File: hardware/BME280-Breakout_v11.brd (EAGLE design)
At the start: 20 x 20 mm, 23 parts, among them IC1 BME280, IC2 LDO-TS9011-3V3, J1 JUMPER2-0603, T1 BSS138PS, T2 BSS138PS, X1 PASSER-07, X2 PASSER-07

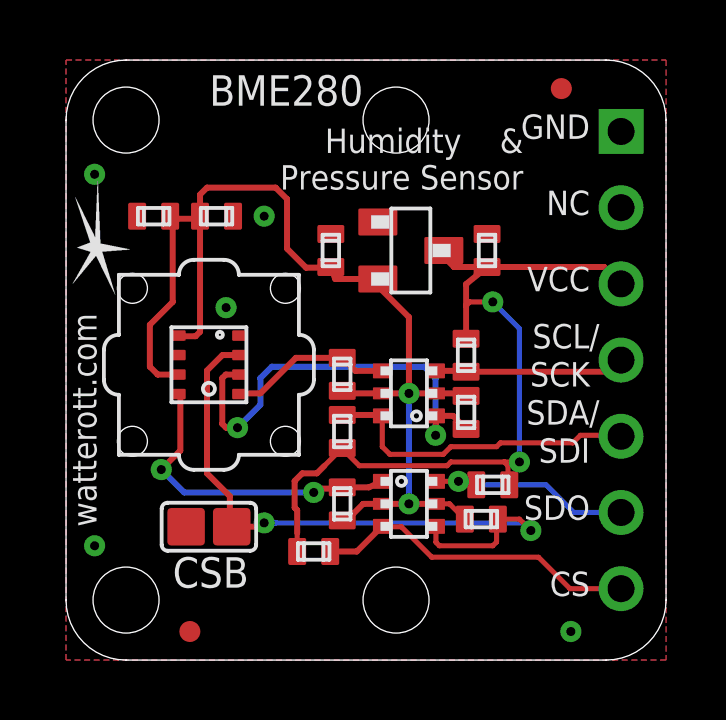
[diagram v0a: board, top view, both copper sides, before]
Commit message: updated schematics
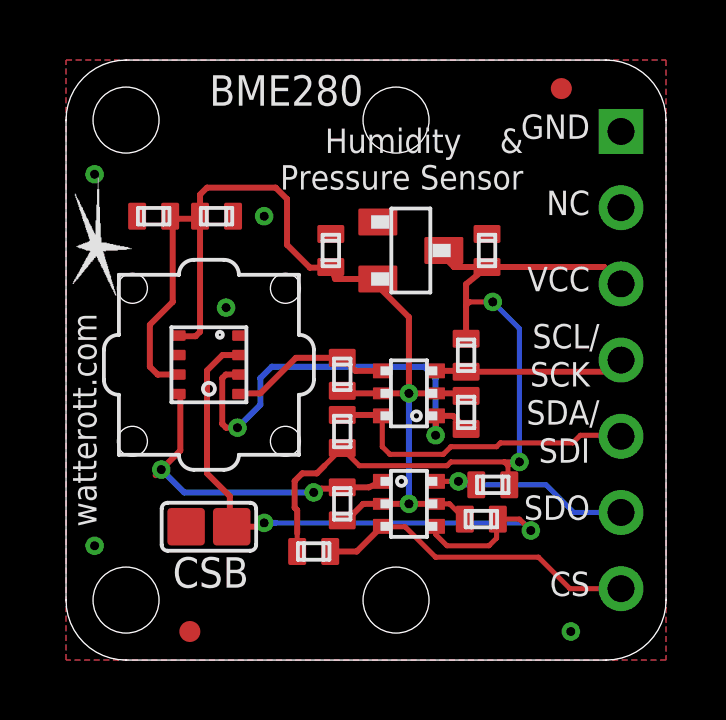
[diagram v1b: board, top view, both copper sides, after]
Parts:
- removed LOGO1: LOGO-S_PLACE_S, we-symbol:SPARK_TPLACE_S
- added LOGO3: LOGO_SPARK-2, we-symbol:SPARK_2MM
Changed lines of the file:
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@@
 <setting verticaltext="up"/>
 </settings>
-<grid distance="0.127" unitdist="mm" unit="mm" style="lines" multiple="1" display="yes" altdistance="0.0125" altunitdist="inch" altunit="inch"/>
+<grid distance="1.27" unitdist="mm" unit="inch" style="lines" multiple="1" display="yes" altdistance="0.0125" altunitdist="inch" altunit="inch"/>
 <layers>
 <layer number="1" name="Top" color="4" fill="1" visible="yes" active="yes"/>
@@
 </class>
 </classes>
-<designrules name="default *">
-<description language="de">&lt;b&gt;EAGLE Design Rules&lt;/b&gt;
-&lt;p&gt;
-Die Standard-Design-Rules sind so gewählt, dass sie für
-die meisten Anwendungen passen. Sollte ihre Platine
-besondere Anforderungen haben, treffen Sie die erforderlichen
-Einstellungen hier und speichern die Design Rules unter
-einem neuen Namen ab.</description>
-<description language="en">&lt;b&gt;EAGLE Design Rules&lt;/b&gt;
-&lt;p&gt;
-The default Design Rules have been set to cover
-a wide range of applications. Your particular design
-may have different requirements, so please make the
-necessary adjustments and save your customized
-design rules under a new name.</description>
+<designrules name="we-dru-2-layer *">
+<description language="de">&lt;b&gt;2 Layer PCB Design Rules&lt;/b&gt;</description>
+<description language="en">&lt;b&gt;2 Layer PCB Design Rules&lt;/b&gt;</description>
 <param name="layerSetup" value="(1*16)"/>
 <param name="mtCopper" value="0.035mm 0.035mm 0.035mm 0.035mm 0.035mm 0.035mm 0.035mm 0.035mm 0.035mm 0.035mm 0.035mm 0.035mm 0.035mm 0.035mm 0.035mm 0.035mm"/>
 <param name="mtIsolate" value="1.5mm 0.15mm 0.2mm 0.15mm 0.2mm 0.15mm 0.2mm 0.15mm 0.2mm 0.15mm 0.2mm 0.15mm 0.2mm 0.15mm 0.2mm"/>
-<param name="mdWireWire" value="6mil"/>
-<param name="mdWirePad" value="6mil"/>
-<param name="mdWireVia" value="6mil"/>
-<param name="mdPadPad" value="6mil"/>
-<param name="mdPadVia" value="6mil"/>
-<param name="mdViaVia" value="6mil"/>
-<param name="mdSmdPad" value="6mil"/>
-<param name="mdSmdVia" value="6mil"/>
-<param name="mdSmdSmd" value="6mil"/>
-<param name="mdViaViaSameLayer" value="8mil"/>
+<param name="mdWireWire" value="0.15mm"/>
+<param name="mdWirePad" value="0.15mm"/>
+<param name="mdWireVia" value="0.15mm"/>
+<param name="mdPadPad" value="0.15mm"/>
+<param name="mdPadVia" value="0.15mm"/>
+<param name="mdViaVia" value="0.15mm"/>
+<param name="mdSmdPad" value="0.1mm"/>
+<param name="mdSmdVia" value="0.1mm"/>
+<param name="mdSmdSmd" value="0.1mm"/>
+<param name="mdViaViaSameLayer" value="0.2mm"/>
 <param name="mnLayersViaInSmd" value="2"/>
-<param name="mdCopperDimension" value="10mil"/>
-<param name="mdDrill" value="8mil"/>
+<param name="mdCopperDimension" value="0.3mm"/>
+<param name="mdDrill" value="0.2mm"/>
 <param name="mdSmdStop" value="0mil"/>
-<param name="msWidth" value="7mil"/>
-<param name="msDrill" value="24mil"/>
+<param name="msWidth" value="0.15mm"/>
+<param name="msDrill" value="0.3mm"/>
 <param name="msMicroVia" value="9.99mm"/>
 <param name="msBlindViaRatio" value="0.5"/>
-<param name="rvPadTop" value="0.25"/>
-<param name="rvPadInner" value="0.25"/>
-<param name="rvPadBottom" value="0.25"/>
+<param name="rvPadTop" value="0.2"/>
+<param name="rvPadInner" value="0.2"/>
+<param name="rvPadBottom" value="0.2"/>
 <param name="rvViaOuter" value="0.25"/>
 <param name="rvViaInner" value="0.25"/>
 <param name="rvMicroViaOuter" value="0.25"/>
 <param name="rvMicroViaInner" value="0.25"/>
-<param name="rlMinPadTop" value="10mil"/>
-<param name="rlMaxPadTop" value="20mil"/>
-<param name="rlMinPadInner" value="10mil"/>
-<param name="rlMaxPadInner" value="20mil"/>
-<param name="rlMinPadBottom" value="10mil"/>
-<param name="rlMaxPadBottom" value="20mil"/>
-<param name="rlMinViaOuter" value="8mil"/>
-<param name="rlMaxViaOuter" value="20mil"/>
-<param name="rlMinViaInner" value="8mil"/>
-<param name="rlMaxViaInner" value="20mil"/>
-<param name="rlMinMicroViaOuter" value="4mil"/>
-<param name="rlMaxMicroViaOuter" value="20mil"/>
-<param name="rlMinMicroViaInner" value="4mil"/>
-<param name="rlMaxMicroViaInner" value="20mil"/>
+<param name="rlMinPadTop" value="0.18mm"/>
+<param name="rlMaxPadTop" value="1mm"/>
+<param name="rlMinPadInner" value="0.18mm"/>
+<param name="rlMaxPadInner" value="1mm"/>
+<param name="rlMinPadBottom" value="0.18mm"/>
+<param name="rlMaxPadBottom" value="1mm"/>
+<param name="rlMinViaOuter" value="0.16mm"/>
+<param name="rlMaxViaOuter" value="1mm"/>
+<param name="rlMinViaInner" value="0.16mm"/>
+<param name="rlMaxViaInner" value="1mm"/>
+<param name="rlMinMicroViaOuter" value="0.1mm"/>
+<param name="rlMaxMicroViaOuter" value="0.5mm"/>
+<param name="rlMinMicroViaInner" value="0.1mm"/>
+<param name="rlMaxMicroViaInner" value="0.5mm"/>
 <param name="psTop" value="-1"/>
 <param name="psBottom" value="-1"/>
@@
 <param name="mvStopFrame" value="1"/>
 <param name="mvCreamFrame" value="0"/>
-<param name="mlMinStopFrame" value="4mil"/>
-<param name="mlMaxStopFrame" value="4mil"/>
+<param name="mlMinStopFrame" value="0.1mm"/>
+<param name="mlMaxStopFrame" value="0.1mm"/>
 <param name="mlMinCreamFrame" value="0mil"/>
 <param name="mlMaxCreamFrame" value="0mil"/>
-<param name="mlViaStopLimit" value="12mil"/>
+<param name="mlViaStopLimit" value="0.5mm"/>
 <param name="srRoundness" value="0"/>
 <param name="srMinRoundness" value="0mil"/>
 <param name="srMaxRoundness" value="0mil"/>
-<param name="slThermalIsolate" value="10mil"/>
+<param name="slThermalIsolate" value="0.25mm"/>
 <param name="slThermalsForVias" value="0"/>
-<param name="dpMaxLengthDifference" value="10mm"/>
+<param name="dpMaxLengthDifference" value="5mm"/>
 <param name="dpGapFactor" value="2.5"/>
 <param name="checkGrid" value="0"/>
-<param name="checkAngle" value="0"/>
-<param name="checkFont" value="1"/>
+<param name="checkAngle" value="1"/>
+<param name="checkFont" value="0"/>
 <param name="checkRestrict" value="1"/>
 <param name="useDiameter" value="13"/>
@@
 <element name="X1" library="we-symbol" package="PASSER_07MM" value="PASSER-07" x="16.51" y="19.05"/>
 <element name="X2" library="we-symbol" package="PASSER_07MM" value="PASSER-07" x="4.1275" y="0.9525"/>
-<element name="LOGO1" library="we-symbol" package="SPARK_TPLACE_S" value="LOGO-S_PLACE_S" x="1.016" y="13.7795" rot="R90"/>
 <element name="LOGO2" library="we-symbol" package="OSHW_6X70" value="OSHW_LOGOX0070" x="4.6355" y="9.144" rot="MR0"/>
 <element name="J1" library="we-rcl" package="JUMPER2-0603" value="JUMPER2-0603" x="4.7625" y="4.445" smashed="yes" rot="R90"/>
 <element name="HOUSING1" library="we-sensor" package="SF2" value="SF2" x="4.7625" y="9.8425"/>
+<element name="LOGO3" library="we-symbol" package="SPARK_2MM" value="LOGO_SPARK-2" x="1.016" y="13.7795" rot="R90"/>
 </elements>
 <signals>
@@
 <wire x1="4.699" y1="15.748" x2="6.985" y2="15.748" width="0.2" layer="1"/>
 <wire x1="6.985" y1="15.748" x2="7.366" y2="15.367" width="0.2" layer="1"/>
-<wire x1="7.366" y1="15.367" x2="7.366" y2="13.716" width="0.2" layer="1"/>
-<wire x1="7.366" y1="13.716" x2="8.001" y2="13.081" width="0.2" layer="1"/>
-<wire x1="8.001" y1="13.081" x2="8.551" y2="13.081" width="0.2" layer="1"/>
+<wire x1="7.366" y1="15.367" x2="7.366" y2="13.843" width="0.2" layer="1"/>
+<wire x1="7.366" y1="13.843" x2="8.128" y2="13.081" width="0.2" layer="1"/>
+<wire x1="8.128" y1="13.081" x2="8.551" y2="13.081" width="0.2" layer="1"/>
 <wire x1="8.551" y1="13.081" x2="8.8265" y2="13.1025" width="0.2" layer="1"/>
 <wire x1="9.2075" y1="4.657" x2="9.356" y2="4.657" width="0.2" layer="1"/>
@@
 <wire x1="5.2145" y1="10.1675" x2="4.699" y2="9.652" width="0.2" layer="1"/>
 <wire x1="4.699" y1="9.652" x2="4.699" y2="6.223" width="0.2" layer="1"/>
-<wire x1="12.33" y1="4.457" x2="12.33" y2="3.926" width="0.17" layer="1"/>
-<wire x1="12.33" y1="3.926" x2="12.446" y2="3.81" width="0.17" layer="1"/>
-<wire x1="12.446" y1="3.81" x2="14.224" y2="3.81" width="0.17" layer="1"/>
-<wire x1="14.224" y1="3.81" x2="14.351" y2="3.937" width="0.17" layer="1"/>
-<wire x1="14.351" y1="3.937" x2="14.351" y2="4.657" width="0.17" layer="1"/>
+<wire x1="12.33" y1="4.457" x2="12.33" y2="4.18" width="0.17" layer="1"/>
+<wire x1="12.33" y1="4.18" x2="12.7" y2="3.81" width="0.17" layer="1"/>
+<wire x1="12.7" y1="3.81" x2="14.097" y2="3.81" width="0.17" layer="1"/>
+<wire x1="14.097" y1="3.81" x2="14.351" y2="4.064" width="0.17" layer="1"/>
+<wire x1="14.351" y1="4.064" x2="14.351" y2="4.657" width="0.17" layer="1"/>
 <wire x1="14.351" y1="4.657" x2="14.393" y2="4.699" width="0.17" layer="1"/>
 <via x="15.494" y="4.318" extent="1-16" drill="0.3"/>
@@
 <wire x1="18.5" y1="2.38" x2="16.797" y2="2.38" width="0.17" layer="1"/>
 <wire x1="16.797" y1="2.38" x2="15.748" y2="3.429" width="0.17" layer="1"/>
-<wire x1="15.748" y1="3.429" x2="12.192" y2="3.429" width="0.17" layer="1"/>
-<wire x1="12.192" y1="3.429" x2="11.176" y2="4.445" width="0.17" layer="1"/>
-<wire x1="11.176" y1="4.445" x2="10.542" y2="4.445" width="0.17" layer="1"/>
+<wire x1="15.748" y1="3.429" x2="12.319" y2="3.429" width="0.17" layer="1"/>
+<wire x1="12.319" y1="3.429" x2="11.303" y2="4.445" width="0.17" layer="1"/>
+<wire x1="11.303" y1="4.445" x2="10.542" y2="4.445" width="0.17" layer="1"/>
 <wire x1="10.542" y1="4.445" x2="10.53" y2="4.457" width="0.17" layer="1"/>
 </signal>
@@
 </signal>
 </signals>
-<errors>
-</errors>
 </board>
 </drawing>
